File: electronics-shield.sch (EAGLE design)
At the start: 82 parts, among them IC1 TLE9201SG, IC2 TLE9201SG, IC3 TLE9201SG, IC4 TLE9201SG, Q2 IRFR5305, U1 STM32F0XX8T, U2 NC7SV157P6X, U3 NC7SV157P6X, U4 V_REG_317SMD, X1 CONNECTOR_PHOENIX_3.81, X2 Listwa zaciskowa rozłączalna 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, Y2 8MHz

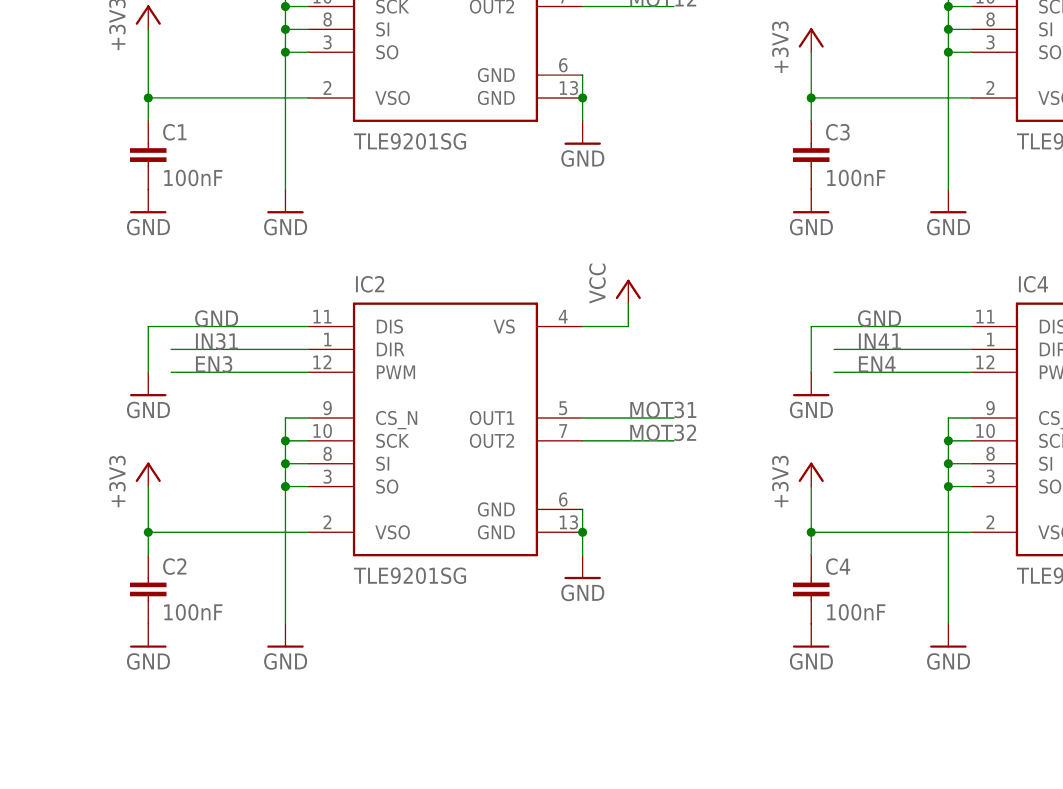
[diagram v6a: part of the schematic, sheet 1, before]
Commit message: Change in description layout
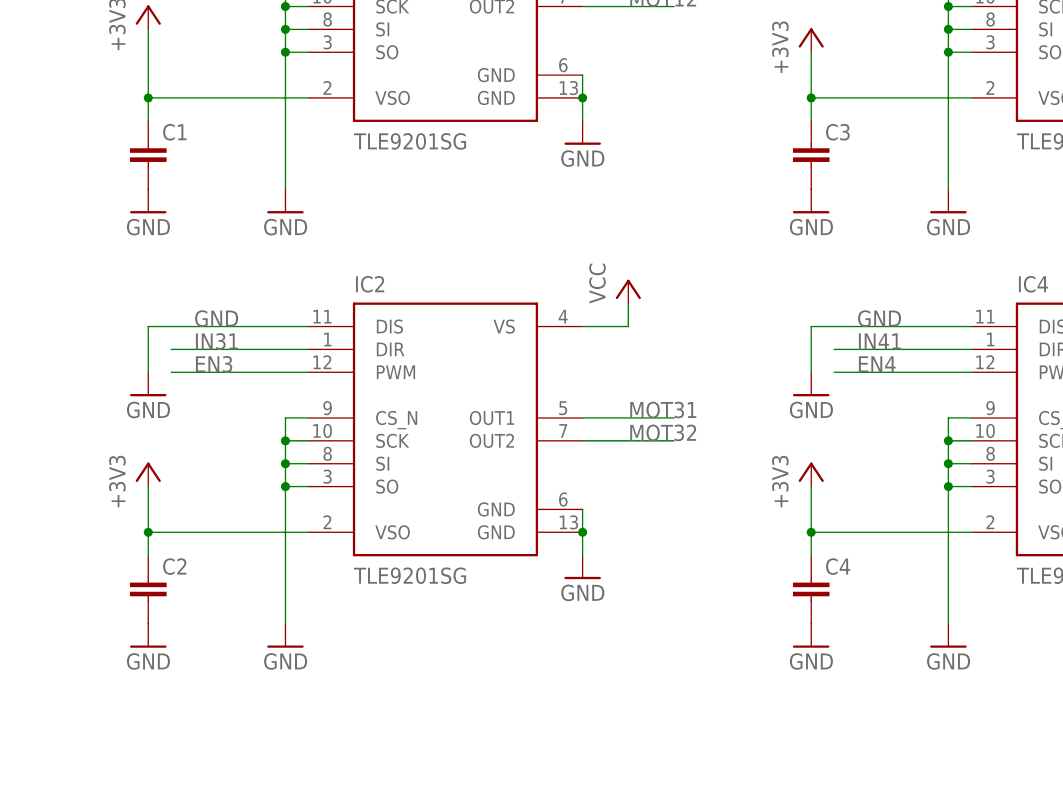
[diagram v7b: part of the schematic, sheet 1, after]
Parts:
- C1, C15, C16, C2, C3, C4: value 100nF -> (none)
- C14, C17: value 22uF -> (none)
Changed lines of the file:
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@@
 <?xml version="1.0" encoding="utf-8"?>
 <!DOCTYPE eagle SYSTEM "eagle.dtd">
-<eagle version="9.3.0">
+<eagle version="9.2.2">
 <drawing>
 <settings>
@@
 <parts>
 <part name="GND39" library="electronics-shield" deviceset="SUPPLY1_GND*?:1" device=""/>
-<part name="R4" library="Kell Ideas" library_urn="urn:adsk.eagle:library:4431361" deviceset="RESISTOR_SMD" device="_0603" package3d_urn="urn:adsk.eagle:package:23555/2"/>
-<part name="R5" library="Kell Ideas" library_urn="urn:adsk.eagle:library:4431361" deviceset="RESISTOR_SMD" device="_0603" package3d_urn="urn:adsk.eagle:package:23555/2"/>
+<part name="R4" library="Kell Ideas" library_urn="urn:adsk.eagle:library:4431361" deviceset="RESISTOR_SMD" device="_0603" package3d_urn="urn:adsk.eagle:package:6534169/2"/>
+<part name="R5" library="Kell Ideas" library_urn="urn:adsk.eagle:library:4431361" deviceset="RESISTOR_SMD" device="_0603" package3d_urn="urn:adsk.eagle:package:6534169/2"/>
 <part name="GND14" library="electronics-shield" deviceset="SUPPLY1_GND*?:1" device=""/>
 <part name="C11" library="Kell Ideas" library_urn="urn:adsk.eagle:library:4431361" deviceset="CAPACITOR_SMD" device="_0603" package3d_urn="urn:adsk.eagle:package:23680/2"/>
@@
 <part name="C8" library="Kell Ideas" library_urn="urn:adsk.eagle:library:4431361" deviceset="CAPACITOR_SMD" device="_0603" package3d_urn="urn:adsk.eagle:package:23680/2"/>
 <part name="GND15" library="electronics-shield" deviceset="SUPPLY1_GND*?:1" device=""/>
-<part name="R2" library="Kell Ideas" library_urn="urn:adsk.eagle:library:4431361" deviceset="RESISTOR_SMD" device="_0603" package3d_urn="urn:adsk.eagle:package:23555/2"/>
-<part name="R3" library="Kell Ideas" library_urn="urn:adsk.eagle:library:4431361" deviceset="RESISTOR_SMD" device="_0603" package3d_urn="urn:adsk.eagle:package:23555/2"/>
-<part name="R1" library="Kell Ideas" library_urn="urn:adsk.eagle:library:4431361" deviceset="RESISTOR_SMD" device="_0603" package3d_urn="urn:adsk.eagle:package:23555/2"/>
+<part name="R2" library="Kell Ideas" library_urn="urn:adsk.eagle:library:4431361" deviceset="RESISTOR_SMD" device="_0603" package3d_urn="urn:adsk.eagle:package:6534169/2"/>
+<part name="R3" library="Kell Ideas" library_urn="urn:adsk.eagle:library:4431361" deviceset="RESISTOR_SMD" device="_0603" package3d_urn="urn:adsk.eagle:package:6534169/2"/>
+<part name="R1" library="Kell Ideas" library_urn="urn:adsk.eagle:library:4431361" deviceset="RESISTOR_SMD" device="_0603" package3d_urn="urn:adsk.eagle:package:6534169/2"/>
 <part name="+3V35" library="electronics-shield" deviceset="SUPPLY1_+3V3" device=""/>
 <part name="GND36" library="electronics-shield" deviceset="SUPPLY1_GND*?:1" device=""/>
@@
 <part name="SUPPLY13" library="electronics-shield" deviceset="SUPPLY2_+7V" device="" value="+7V/1"/>
 <part name="SUPPLY14" library="electronics-shield" deviceset="SUPPLY2_+7V" device="" value="+7V/2"/>
-<part name="PCB1" library="Kell Ideas" library_urn="urn:adsk.eagle:library:4431361" deviceset="RASPBERRY_PI_B+" device="" package3d_urn="urn:adsk.eagle:package:5691962/2" value="Listwa stykowa 2.54mm prosta 2x20 (40-pin), wydłużona"/>
+<part name="PCB1" library="Kell Ideas" library_urn="urn:adsk.eagle:library:4431361" deviceset="RASPBERRY_PI_B+" device="" package3d_urn="urn:adsk.eagle:package:5691962/4" value="Listwa stykowa 2.54mm prosta 2x20 (40-pin), wydłużona"/>
 <part name="FRAME6" library="electronics-shield" deviceset="SYNERGICZNE_RAMKA_SYNERGIA" device=""/>
 <part name="FRAME2" library="electronics-shield" deviceset="SYNERGICZNE_RAMKA_SYNERGIA" device=""/>
@@
 <part name="IC3" library="Kell Ideas" library_urn="urn:adsk.eagle:library:4431361" deviceset="TLE9201SG" device="" package3d_urn="urn:adsk.eagle:package:4698922/2"/>
 <part name="IC4" library="Kell Ideas" library_urn="urn:adsk.eagle:library:4431361" deviceset="TLE9201SG" device="" package3d_urn="urn:adsk.eagle:package:4698922/2"/>
-<part name="C1" library="Kell Ideas" library_urn="urn:adsk.eagle:library:4431361" deviceset="CAPACITOR_SMD" device="_0603" package3d_urn="urn:adsk.eagle:package:23680/2" value="100nF"/>
-<part name="C2" library="Kell Ideas" library_urn="urn:adsk.eagle:library:4431361" deviceset="CAPACITOR_SMD" device="_0603" package3d_urn="urn:adsk.eagle:package:23680/2" value="100nF"/>
-<part name="C3" library="Kell Ideas" library_urn="urn:adsk.eagle:library:4431361" deviceset="CAPACITOR_SMD" device="_0603" package3d_urn="urn:adsk.eagle:package:23680/2" value="100nF"/>
-<part name="C4" library="Kell Ideas" library_urn="urn:adsk.eagle:library:4431361" deviceset="CAPACITOR_SMD" device="_0603" package3d_urn="urn:adsk.eagle:package:23680/2" value="100nF"/>
+<part name="C1" library="Kell Ideas" library_urn="urn:adsk.eagle:library:4431361" deviceset="CAPACITOR_SMD" device="_0603" package3d_urn="urn:adsk.eagle:package:23680/2"/>
+<part name="C2" library="Kell Ideas" library_urn="urn:adsk.eagle:library:4431361" deviceset="CAPACITOR_SMD" device="_0603" package3d_urn="urn:adsk.eagle:package:23680/2"/>
+<part name="C3" library="Kell Ideas" library_urn="urn:adsk.eagle:library:4431361" deviceset="CAPACITOR_SMD" device="_0603" package3d_urn="urn:adsk.eagle:package:23680/2"/>
+<part name="C4" library="Kell Ideas" library_urn="urn:adsk.eagle:library:4431361" deviceset="CAPACITOR_SMD" device="_0603" package3d_urn="urn:adsk.eagle:package:23680/2"/>
 <part name="JP1" library="Kell Ideas" library_urn="urn:adsk.eagle:library:4431361" deviceset="PINHD-1X3" device="_DNP" package3d_urn="urn:adsk.eagle:package:4691208/2" value="Listwa kołkowa 2.54mm prosta 1x3 (3pin)"/>
 <part name="JP2" library="Kell Ideas" library_urn="urn:adsk.eagle:library:4431361" deviceset="PINHD-1X3" device="_DNP" package3d_urn="urn:adsk.eagle:package:4691208/2" value="Listwa kołkowa 2.54mm prosta 1x3 (3pin)"/>
@@
 <part name="X1" library="Kell Ideas" library_urn="urn:adsk.eagle:library:4431361" deviceset="CONNECTOR_PHOENIX_3.81" device="" package3d_urn="urn:adsk.eagle:package:4699073/2"/>
 <part name="LED1" library="audio amplifier example" library_urn="urn:adsk.eagle:library:970892" deviceset="LED" device="CHIPLED_0603" package3d_urn="urn:adsk.eagle:package:970932/2"/>
-<part name="R9" library="Kell Ideas" library_urn="urn:adsk.eagle:library:4431361" deviceset="RESISTOR_SMD" device="_0603" package3d_urn="urn:adsk.eagle:package:23555/2"/>
+<part name="R9" library="Kell Ideas" library_urn="urn:adsk.eagle:library:4431361" deviceset="RESISTOR_SMD" device="_0603" package3d_urn="urn:adsk.eagle:package:6534169/2"/>
 <part name="P+6" library="supply1" library_urn="urn:adsk.eagle:library:371" deviceset="VCC" device=""/>
 <part name="GND44" library="supply1" library_urn="urn:adsk.eagle:library:371" deviceset="GND" device=""/>
@@
 <part name="P+16" library="electronics-shield" deviceset="SUPPLY1_+5V" device=""/>
 <part name="U4" library="Kell Ideas" library_urn="urn:adsk.eagle:library:4431361" deviceset="V_REG_317" device="SMD" package3d_urn="urn:adsk.eagle:package:39069/1"/>
-<part name="C15" library="Kell Ideas" library_urn="urn:adsk.eagle:library:4431361" deviceset="CAPACITOR_SMD" device="_0603" package3d_urn="urn:adsk.eagle:package:23680/2" value="100nF"/>
-<part name="C16" library="Kell Ideas" library_urn="urn:adsk.eagle:library:4431361" deviceset="CAPACITOR_SMD" device="_0603" package3d_urn="urn:adsk.eagle:package:23680/2" value="100nF"/>
-<part name="C14" library="Kell Ideas" library_urn="urn:adsk.eagle:library:4431361" deviceset="CAPACITOR_SMD" device="_0603" package3d_urn="urn:adsk.eagle:package:23680/2" value="22uF"/>
-<part name="C17" library="Kell Ideas" library_urn="urn:adsk.eagle:library:4431361" deviceset="CAPACITOR_SMD" device="_0603" package3d_urn="urn:adsk.eagle:package:23680/2" value="22uF"/>
+<part name="C15" library="Kell Ideas" library_urn="urn:adsk.eagle:library:4431361" deviceset="CAPACITOR_SMD" device="_0603" package3d_urn="urn:adsk.eagle:package:23680/2"/>
+<part name="C16" library="Kell Ideas" library_urn="urn:adsk.eagle:library:4431361" deviceset="CAPACITOR_SMD" device="_0603" package3d_urn="urn:adsk.eagle:package:23680/2"/>
+<part name="C14" library="Kell Ideas" library_urn="urn:adsk.eagle:library:4431361" deviceset="CAPACITOR_SMD" device="_0603" package3d_urn="urn:adsk.eagle:package:23680/2"/>
+<part name="C17" library="Kell Ideas" library_urn="urn:adsk.eagle:library:4431361" deviceset="CAPACITOR_SMD" device="_0603" package3d_urn="urn:adsk.eagle:package:23680/2"/>
 <part name="GND7" library="supply1" library_urn="urn:adsk.eagle:library:371" deviceset="GND" device=""/>
 <part name="GND27" library="supply1" library_urn="urn:adsk.eagle:library:371" deviceset="GND" device=""/>
@@
 <part name="+3V2" library="supply1" library_urn="urn:adsk.eagle:library:371" deviceset="+3V3" device=""/>
 <part name="P+19" library="supply1" library_urn="urn:adsk.eagle:library:371" deviceset="+5V" device=""/>
-<part name="R12" library="Kell Ideas" library_urn="urn:adsk.eagle:library:4431361" deviceset="RESISTOR_SMD" device="_0603" package3d_urn="urn:adsk.eagle:package:23555/2"/>
-<part name="R13" library="Kell Ideas" library_urn="urn:adsk.eagle:library:4431361" deviceset="RESISTOR_SMD" device="_0603" package3d_urn="urn:adsk.eagle:package:23555/2"/>
+<part name="R12" library="Kell Ideas" library_urn="urn:adsk.eagle:library:4431361" deviceset="RESISTOR_SMD" device="_0603" package3d_urn="urn:adsk.eagle:package:6534169/2"/>
+<part name="R13" library="Kell Ideas" library_urn="urn:adsk.eagle:library:4431361" deviceset="RESISTOR_SMD" device="_0603" package3d_urn="urn:adsk.eagle:package:6534169/2"/>
 <part name="GND31" library="electronics-shield" deviceset="SUPPLY1_GND*?:1" device=""/>
 <part name="P+5" library="supply1" library_urn="urn:adsk.eagle:library:371" deviceset="VCC" device=""/>
